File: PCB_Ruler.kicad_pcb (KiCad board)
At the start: 2 copper layers, 100.5 x 27 mm, 118 parts, among them Q1 SOT23-3, Q10 SOT89, Q11 SOT886, Q12 SOT963, Q13 SSOP-16, Q14 SSOP-8, Q15 SOT1113, Q16 SOT665, Q17 SO-8, Q18 QFNx24, Q19 QFPx100_0.5, Q2 SOT23-5, Q20 QFPx32, Q21 QFPx32_0.8, Q22 QFPx100, Q23 SOIC, Q24 TSOP-48, Q25 BGA_DDR4, Q26 BGA_10x, Q27 BGA_4x, Q28 QNFx20, Q29 QNFx40, Q3 SOT323, Q30 QNFx48, Q31 QNFx64, Q32 QFPx48, Q33 QFPx64, Q34 BGA_5, Q35 BGA_78x, Q36 BGA_4, Q37 BGA_6x, Q38 BGA_5x_1.27, Q39 BGA_15x_0.65, Q4 SOT353, Q40 QNFx32, Q41 QNFx12, Q42 SC-59, Q5 SOT553, Q6 DPAK, Q7 DP2AK, Q8 LFPAK, Q9 SOT223, U1 1.00, U10 5mm, U11 6mm, U12 7mm, U13 8mm, U14 9mm, U15 3_10in, U16 0_16in, U17 1_16in, U18 2_16in, U19 3_16in, U2 1.27, U20 0_10in, U21 1_10in, U22 2_10in, U3 2.00, U4 2.54, U5 0mm, U6 1mm, U7 2mm, U8 3mm, U9 4mm

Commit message: Moved some parts around
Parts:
- added Q43: BGA_8, Package_BGA:Texas_DSBGA-8_1.43x1.41mm_Layout3x3_P0.5mm, B.Cu at (169.1, 111.8)
- moved Q34 3.47 mm to (165.7, 111.9)
- moved Q36 3.02 mm to (167.2, 111.9)
- moved Q27 2.10 mm to (166.5, 101.8)
- moved E$54 0.83 mm to (162.3, 112.7)
- moved Q18 0.51 mm to (98.4, 100.6)
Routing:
- net /Pin1: track 486.3 -> 506.8 mm
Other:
- board text added: "BGA4"
- board text added: "BGA5"
- board text added: "BGA8 P0.5"
- board text added: "P0.4"
- board text removed: "BGA4 P0.4"
- board text removed: "BGA5 P0.4"

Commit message: Move a few things around
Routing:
- net /Pin1: track 506.8 -> 514.1 mm

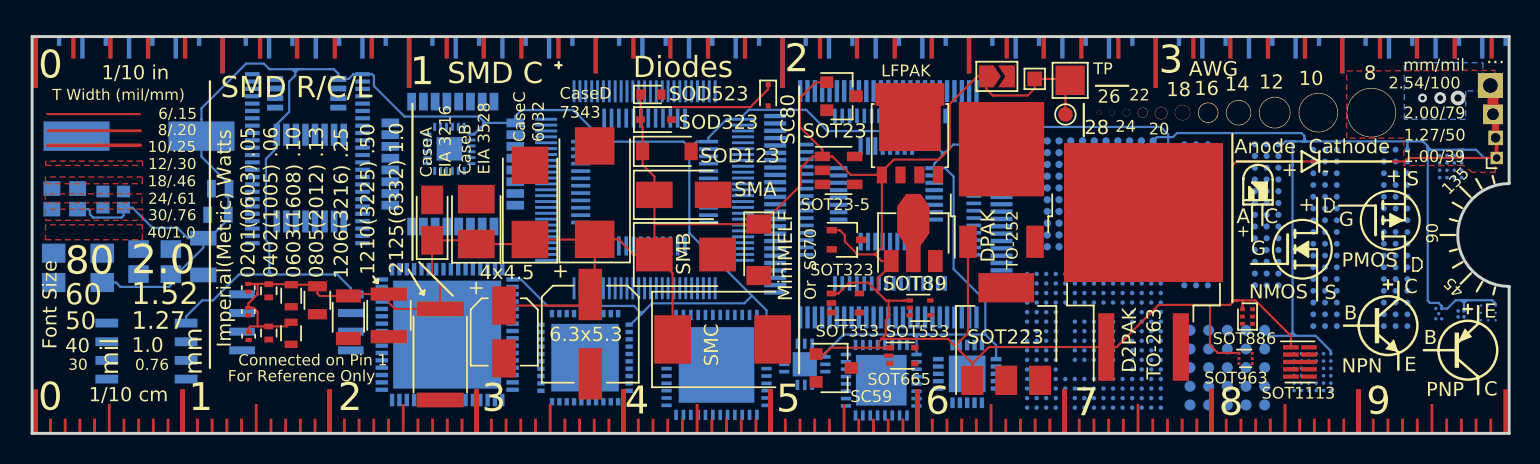
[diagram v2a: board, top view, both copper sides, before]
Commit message: v2.1 VSON - USON + X2 update
Added VSON WSON USON and X2 devices. Also added 10 pin triode and removed big TO pad to make place for it. Removed Transistor symbols added text hints. Minor retuches to silkscreen positioning. KiCad 9.0.3
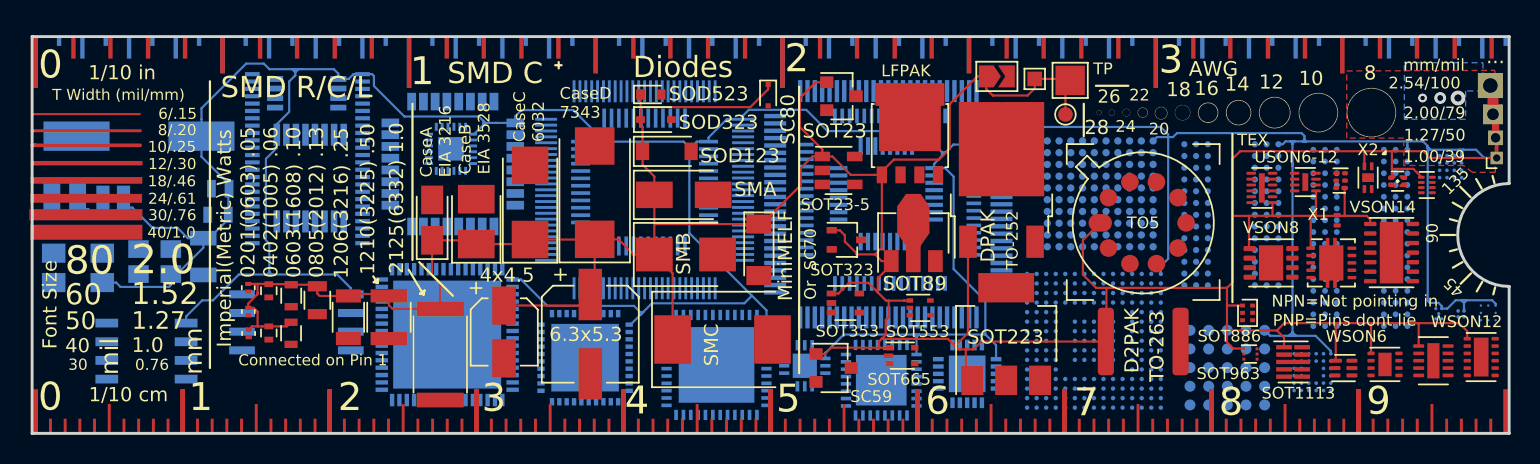
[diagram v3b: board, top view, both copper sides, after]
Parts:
- removed E$50: , PCB_Ruler:NMOS-SYMB
- removed E$51: , PCB_Ruler:PMOS-SYMB
- removed E$52: , Adafruit PCB Reference Ruler:DIODE-SYMB
- removed E$53: , PCB_Ruler:LED-GUIDE
- removed E$54: , PCB_Ruler:NPN-SYMB
- removed E$59: , PCB_Ruler:PNP-SYMB
- removed Q7: DP2AK, TO_SOT_Packages_SMD:TO-263-2
- added REF**: TO-263-3_TabPin4, Package_TO_SOT_SMD:TO-263-3_TabPin4, F.Cu at (145.6, 106.1)
- added TO5: TO-5-10, Package_TO_SOT_THT:TO-5-10, F.Cu at (142.7, 105.7)
- added USON6: Texas_USON-6_1x1.45mm_P0.5mm_SMD, Package_SON:Texas_USON-6_1x1.45mm_P0.5mm_SMD, F.Cu at (159.0, 102.8)
- added USON6-12: Nexperia_HUSON-12_USON-12-1EP_1.35x2.5mm_P0.4mm_EP0.4x2mm, Package_SON:Nexperia_HUSON-12_USON-12-1EP_1.35x2.5mm_P0.4mm_EP0.4x2mm, F.Cu at (153.7, 103.3)
- added USON8: Nexperia_HUSON-8_USON-8-1EP_1.35x1.7mm_P0.4mm_EP0.4x1.2mm, Package_SON:Nexperia_HUSON-8_USON-8-1EP_1.35x1.7mm_P0.4mm_EP0.4x1.2mm, F.Cu at (156.6, 102.9)
- added VSON10: Texas_DRC0010J, Package_SON:Texas_DRC0010J, F.Cu at (158.4, 108.4)
- added VSON14: VSON-14-1EP_3x4.45mm_P0.65mm_EP1.6x4.2mm, Package_SON:VSON-14-1EP_3x4.45mm_P0.65mm_EP1.6x4.2mm, F.Cu at (162.5, 107.7)
- added VSON8: VSON-8-1EP_3x3mm_P0.65mm_EP1.65x2.4mm, Package_SON:VSON-8-1EP_3x3mm_P0.65mm_EP1.65x2.4mm, F.Cu at (154.3, 108.4)
- added WSON10: WSON-10-1EP_2x3mm_P0.5mm_EP0.84x2.4mm, Package_SON:WSON-10-1EP_2x3mm_P0.5mm_EP0.84x2.4mm, F.Cu at (165.3, 115.1)
- added WSON12: WSON-12-1EP_3x2mm_P0.5mm_EP1x2.65, Package_SON:WSON-12-1EP_3x2mm_P0.5mm_EP1x2.65, F.Cu at (168.6, 114.8)
- added WSON6: WSON6_1.5x1.5mm_P0.5mm, Package_SON:WSON-6_1.5x1.5mm_P0.5mm, F.Cu at (159.2, 115.6)
- added WSON8: WSON-8-1EP_2x2mm_P0.5mm_EP0.9x1.6mm, Package_SON:WSON-8-1EP_2x2mm_P0.5mm_EP0.9x1.6mm, F.Cu at (162.1, 115.3)
- added X1: Texas_DPY0002A_0.6x1mm_P0.65mm, Package_SON:Texas_DPY0002A_0.6x1mm_P0.65mm, F.Cu at (158.8, 105.5)
- added X2: Texas_X2SON-5_0.8x0.8mm_P0.48mm, Package_SON:Texas_X2SON-5_0.8x0.8mm_P0.48mm, F.Cu at (162.9, 102.8)
- added X2SON4: Texas_X2SON-4-1EP_1.1x1.4mm_P0.5mm_EP0.8x0.6mm, Package_SON:Texas_X2SON-4-1EP_1.1x1.4mm_P0.5mm_EP0.8x0.6mm, F.Cu at (160.9, 102.6)
- added X2SON8: X2SON-8_1.4x1mm_P0.35mm, Package_SON:X2SON-8_1.4x1mm_P0.35mm, F.Cu at (164.9, 103.1)
- moved Q15 0.46 mm to (155.8, 115.1)
- moved Q12 0.45 mm to (152.9, 114.6)
- moved Q11 0.25 mm to (152.7, 111.8)
- moved R3 0.18 mm to (84.7, 113.2)
- moved R10 0.13 mm to (94.3, 112.1)
- moved Q18 0.11 mm to (98.5, 100.6)
- moved Q41 0.10 mm to (122.6, 115.4)
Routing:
- net /Pin1: track 514.1 -> 565.0 mm
- net (no net): track 18.9 -> 22.1 mm
- removed copper zone on F.Cu, net (none)
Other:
- net class Default removed
- board text added: "1 inch=2.54 mm"
- board text added: "BGA32P0.5"
- board text added: "Modified Adafruit PCB Ruler v2.1 MYoung&BaTl"
- board text added: "NPN=Not pointing in"
- board text added: "PNP=Pins dont lie"
- board text added: "TEX"
- board text added: "XTAL"
- board text removed: "1 in = 2.54 mm"
- board text removed: "BGA32 P0.5"
- board text removed: "For Reference Only"
- board text removed: "Modified Adafruit PCB Ruler v2 M Young"
- board text removed: "OSC/XTAL"

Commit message: Teardrops
Teardrops and more minor adjustments to silkscreen
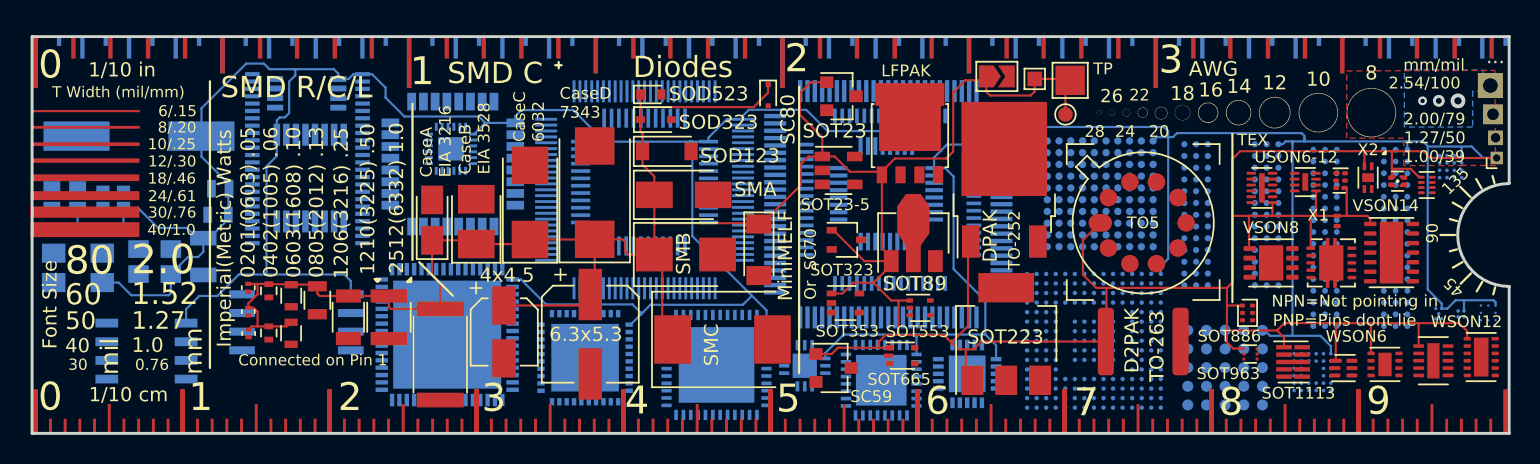
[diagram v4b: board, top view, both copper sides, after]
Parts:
- moved Q6 0.19 mm to (136.2, 102.8)
- moved Q38 0.15 mm to (151.2, 115.5)
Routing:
- net /Pin1: track 565.0 -> 555.9 mm
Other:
- board text added: "2.5x2"
- board text added: "2512(6332) 1.0"
- board text added: "BGA16"
- board text added: "P0.5"
- board text added: "P=IU"
- board text removed: "2.5x2."
- board text removed: "2125(6332) 1.0"
- board text removed: "BGA16 P0.5"
- board text removed: "P=IV"

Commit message: More edits
Swapped copper for silkscreen for even numbered pads in TEX section
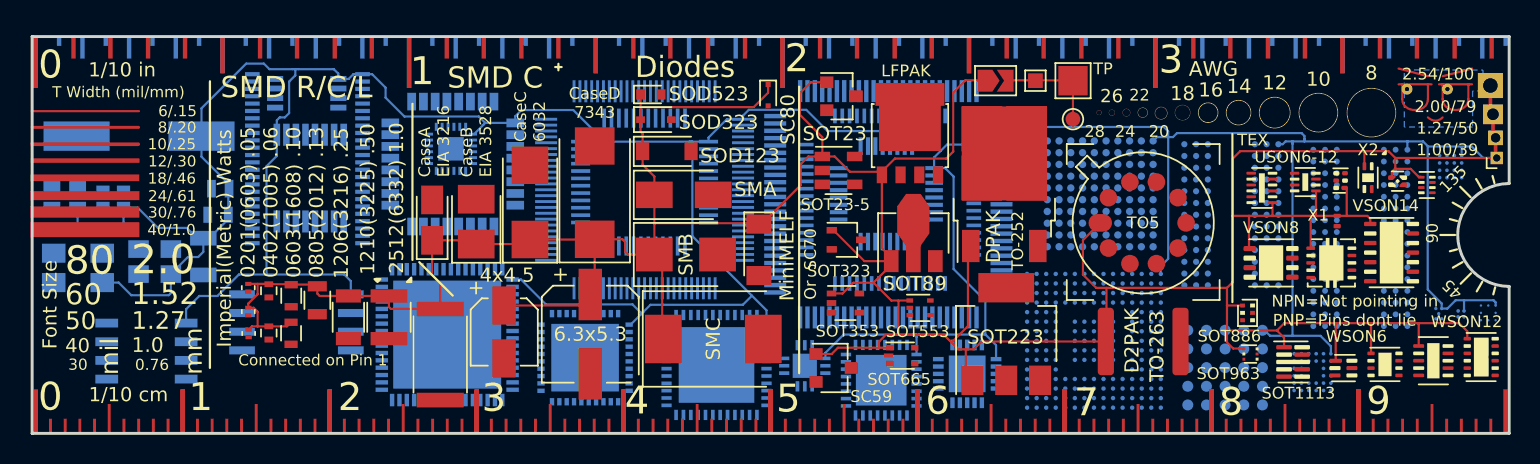
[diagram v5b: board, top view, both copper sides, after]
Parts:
- added REF**: CirnoFumo, Cirno:CirnoFumo, F.Cu at (163.0, 96.2)
- moved D7 0.63 mm to (116.3, 113.6)
- moved TP2 0.60 mm to (140.8, 98.6)
- moved JP1 0.30 mm to (135.6, 96.0)
- moved Q6 0.30 mm to (136.2, 103.0)
- moved TP3 0.20 mm to (140.8, 96.0)
- moved TP1 0.13 mm to (138.3, 96.0)
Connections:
- JP1 pad 2: (no net) -> /Pin1
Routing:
- net /Pin1: track 555.9 -> 556.8 mm, vias 3 -> 0
- removed copper zone on F.Cu, net /Pin1
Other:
- rule pad_to_mask_clearance: 0.051 -> 0.038
- rule solder_mask_min_width: 0.25 -> 0.2
- board text removed: "mm/mil"

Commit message: Final tweaks
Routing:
- removed copper zone on B.Cu, net /Pin1
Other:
- board text added: "BGA 16"
- board text removed: "BGA16"
